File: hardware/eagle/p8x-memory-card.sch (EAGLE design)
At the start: 10 parts, among them J1 DIN41612-96M, U1 28C256-15, U2 62256-70, U3 74HCT245, U4 74HCT30, U5 74HCT138-DOE, U6 74HCT138-DLD, U7 74HCT00, U8 74HCT32, U9 74HCT08

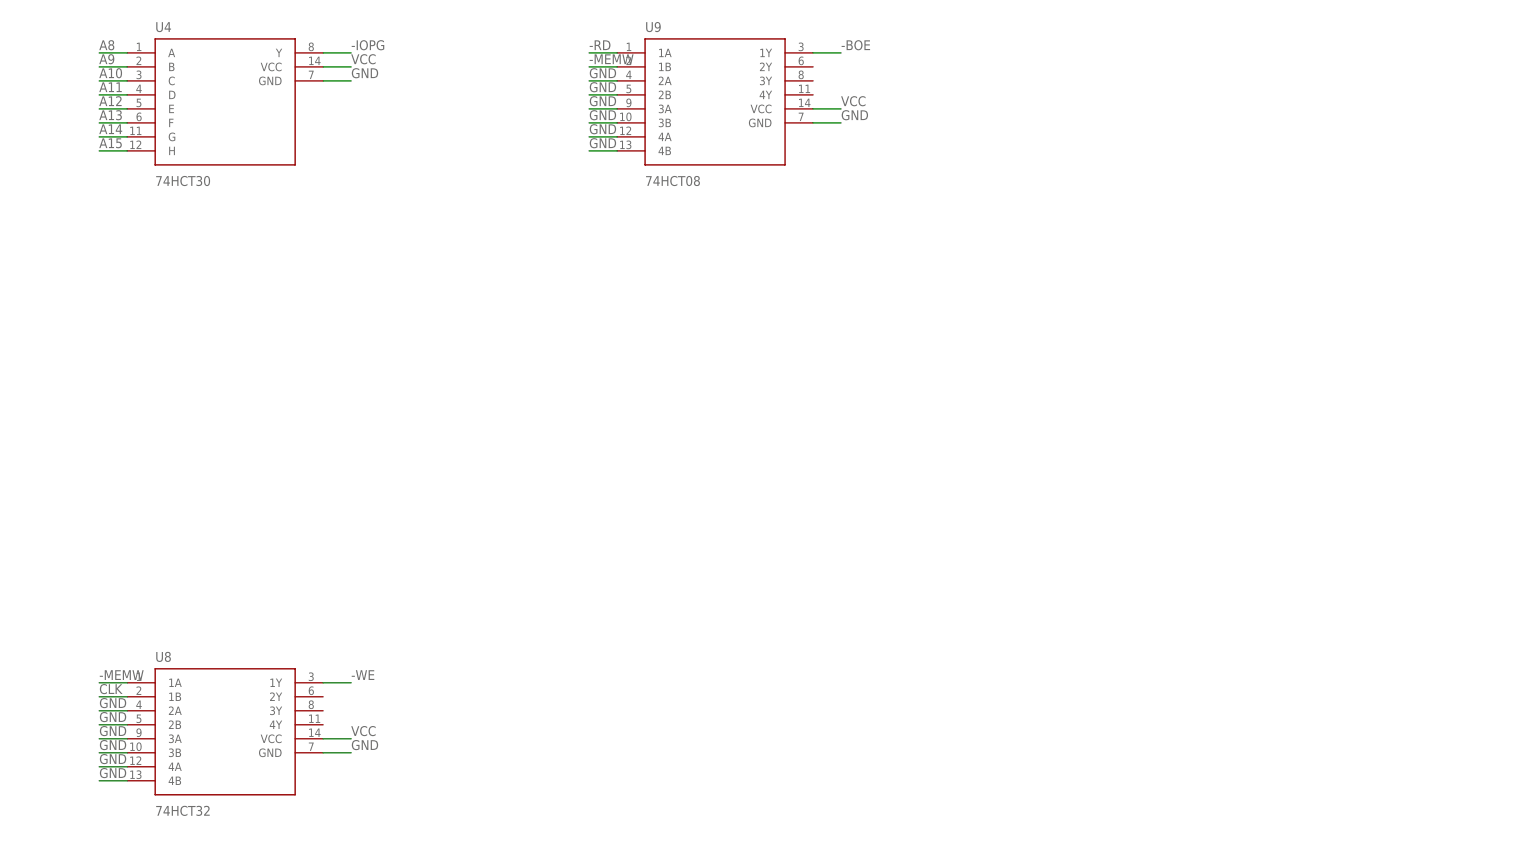
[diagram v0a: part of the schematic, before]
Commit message: Memory card: ROM/RAM/RD/WR access LEDs replace SEL; traditional schematic PDFs; backlog + standards updates
- Select LEDs gated with -BOE (real accesses, not idle decode); spare U8/U9 gates as drivers
- Standards sec.9 allows finer-grained LED sets; fab checklist updated
- New traditional-style schematic PDFs + their render scripts (generators/)
- Backlog: DIN flange holes, board mounting holes, backplane PWR LED placement review
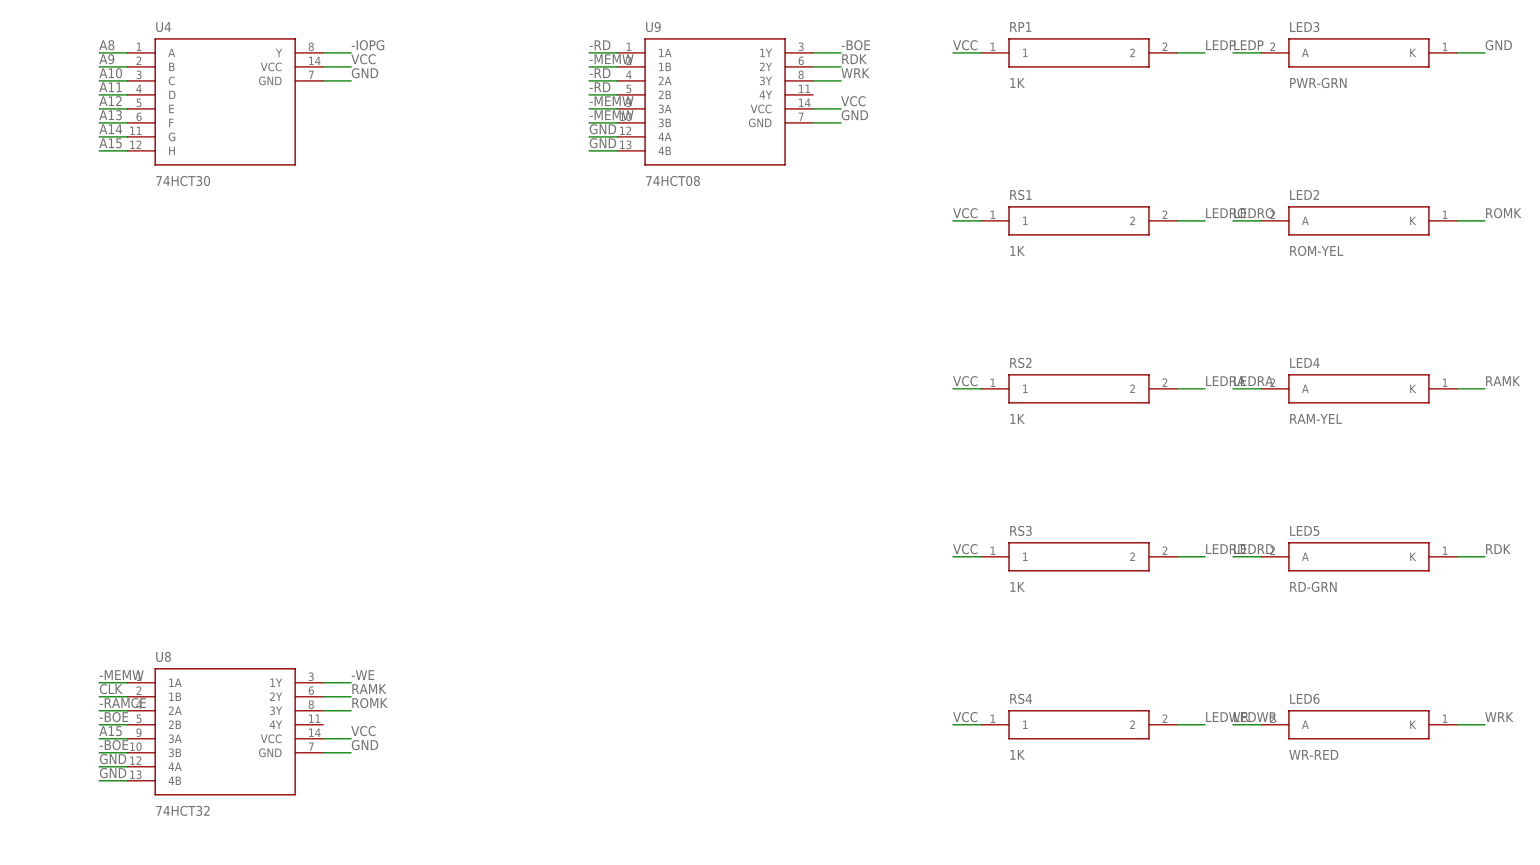
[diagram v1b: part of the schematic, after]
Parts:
- added LED2: ROM-YEL, p8x:LED
- added LED3: PWR-GRN, p8x:LED
- added LED4: RAM-YEL, p8x:LED
- added LED5: RD-GRN, p8x:LED
- added LED6: WR-RED, p8x:LED
- added RP1, RS1, RS2, RS3, RS4: 1K, p8x:RES
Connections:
- new net LEDP: LED3.A, RP1.2
- new net LEDRA: LED4.A, RS2.2
- new net LEDRD: LED5.A, RS3.2
- new net LEDRO: LED2.A, RS1.2
- new net LEDWR: LED6.A, RS4.2
- new net RAMK: LED4.K, U8.2Y
- new net RDK: LED5.K, U9.2Y
- new net ROMK: LED2.K, U8.3Y
- new net WRK: LED6.K, U9.3Y
- net -BOE: now also U8.2B, U8.3B
- net -MEMW: now also U9.3A, U9.3B
- net -RAMCE: now also U8.2A
- net -RD: now also U9.2A, U9.2B
- net A15: now also U8.3A
- net GND: now also LED3.K; no longer U8.2A, U8.2B, U8.3A, U8.3B, U9.2A, U9.2B, U9.3A, U9.3B
- net VCC: now also RP1.1, RS1.1, RS2.1, RS3.1, RS4.1

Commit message: redo all files
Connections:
- net GND: no longer J1.B27, J1.B28, J1.B29, J1.B30
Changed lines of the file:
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@@
 <wire x1="17.78" y1="-106.68" x2="12.70" y2="-106.68" width="0.1524" layer="91"/>
 <label x="12.70" y="-106.17" size="1.778" layer="95"/></segment>
-<segment><pinref part="J1" gate="G$1" pin="B27"/>
-<wire x1="17.78" y1="-109.22" x2="12.70" y2="-109.22" width="0.1524" layer="91"/>
-<label x="12.70" y="-108.71" size="1.778" layer="95"/></segment>
-<segment><pinref part="J1" gate="G$1" pin="B28"/>
-<wire x1="17.78" y1="-111.76" x2="12.70" y2="-111.76" width="0.1524" layer="91"/>
-<label x="12.70" y="-111.25" size="1.778" layer="95"/></segment>
-<segment><pinref part="J1" gate="G$1" pin="B29"/>
-<wire x1="17.78" y1="-114.30" x2="12.70" y2="-114.30" width="0.1524" layer="91"/>
-<label x="12.70" y="-113.79" size="1.778" layer="95"/></segment>
-<segment><pinref part="J1" gate="G$1" pin="B30"/>
-<wire x1="17.78" y1="-116.84" x2="12.70" y2="-116.84" width="0.1524" layer="91"/>
-<label x="12.70" y="-116.33" size="1.778" layer="95"/></segment>
 <segment><pinref part="U1" gate="G$1" pin="GND"/>
 <wire x1="149.86" y1="7.62" x2="154.94" y2="7.62" width="0.1524" layer="91"/>
